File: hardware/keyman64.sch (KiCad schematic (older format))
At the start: 28 parts, among them IC1 ATMEGA1284P-P, P1 SERIAL, P2 CIA1, P3 KEYBOARD, P4 USER, P5 POWER, P6 USB, SW1 RESET, SW2 BOOTLOADER, U1 7400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

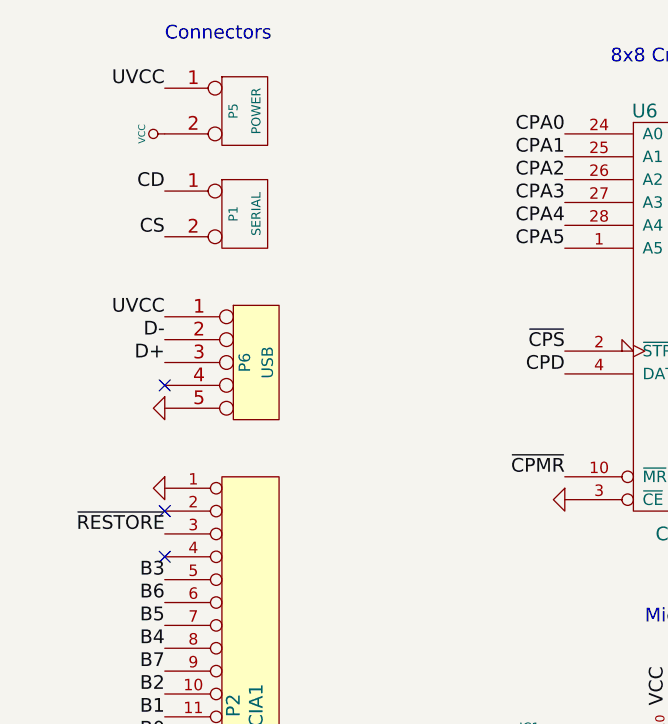
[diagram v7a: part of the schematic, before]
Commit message: Hardware: Added option to use VCC from mainboard keyboard header
This is in case you want to make a custom cable to connect the keyman64 to
the C64 mainboard keyboard header, in which case you might want to use
PIN 4 of the mainboard header to provide VCC.
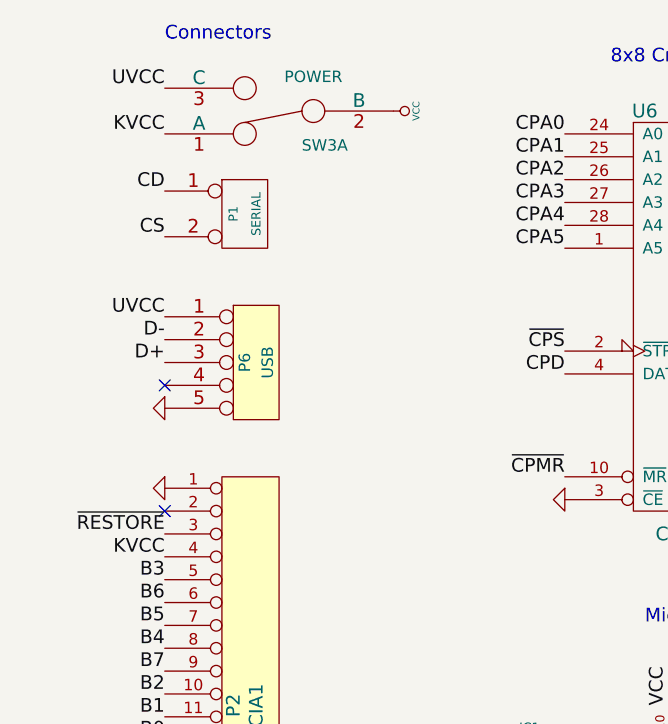
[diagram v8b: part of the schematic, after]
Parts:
- removed P5: POWER, symbol CONN_2
- added SW3: POWER, ~, symbol DUAL_SWITCH_INV
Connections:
- net UVCC: now also SW3.3 (C)
- net VCC: now also SW3.2 (B)
- net KVCC: now reaches P2.4 (P4)
- net KVCC: now also SW3.1 (A)
- no-connect marks 9 -> 8
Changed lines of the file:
@@
 Sheet 1 1
 Title "Programmable C64 Keyboard Interceptor and Hardware Controller"
-Date "17 oct 2015"
+Date "23 oct 2015"
 Rev "2"
 Comp "Henning Bekel"
@@
 Text Label 900  1900 2    60   ~ 0
 UVCC
-$Comp
-L CONN_2 P5
-U 1 1 5622005B
-P 1250 1000
-F 0 "P5" V 1200 1000 40  0000 C CNN
-F 1 "POWER" V 1300 1000 40  0000 C CNN
-F 2 "" H 1250 1000 60  0000 C CNN
-F 3 "" H 1250 1000 60  0000 C CNN
-	1    1250 1000
-	1    0    0    -1
-$EndComp
 Text Label 900  900  2    60   ~ 0
 UVCC
@@
 L VCC #PWR045
 U 1 1 5622006F
-P 900 1100
-F 0 "#PWR045" H 900 1200 30  0001 C CNN
-F 1 "VCC" H 900 1200 30  0000 C CNN
-F 2 "" H 900 1100 60  0000 C CNN
-F 3 "" H 900 1100 60  0000 C CNN
-	1    900  1100
-	0    -1   -1   0
-$EndComp
-NoConn ~ 900  2950
+P 1900 1000
+F 0 "#PWR045" H 1900 1100 30  0001 C CNN
+F 1 "VCC" H 1900 1100 30  0000 C CNN
+F 2 "" H 1900 1000 60  0000 C CNN
+F 3 "" H 1900 1000 60  0000 C CNN
+	1    1900 1000
+	0    1    1    0
+$EndComp
+$Comp
+L DUAL_SWITCH_INV SW3
+U 1 1 562A2E46
+P 1400 1000
+F 0 "SW3" H 1200 1150 50  0000 C CNN
+F 1 "POWER" H 1250 850 50  0000 C CNN
+F 2 "~" H 1400 1000 60  0000 C CNN
+F 3 "~" H 1400 1000 60  0000 C CNN
+	1    1400 1000
+	-1   0    0    1
+$EndComp
+Text Label 900  1100 2    60   ~ 0
+KVCC
+Text Label 900  2950 2    60   ~ 0
+KVCC
 $EndSCHEMATC
